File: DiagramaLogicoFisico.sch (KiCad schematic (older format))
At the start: 18 parts, among them J1 Conn_01x02, J2 Conn_01x03, J3 Conn_01x03, J4 Conn_01x04, J5 Conn_01x05, U1 TC1262-33, U2 DSPIC33EP128GM604, Y1 7Mhz

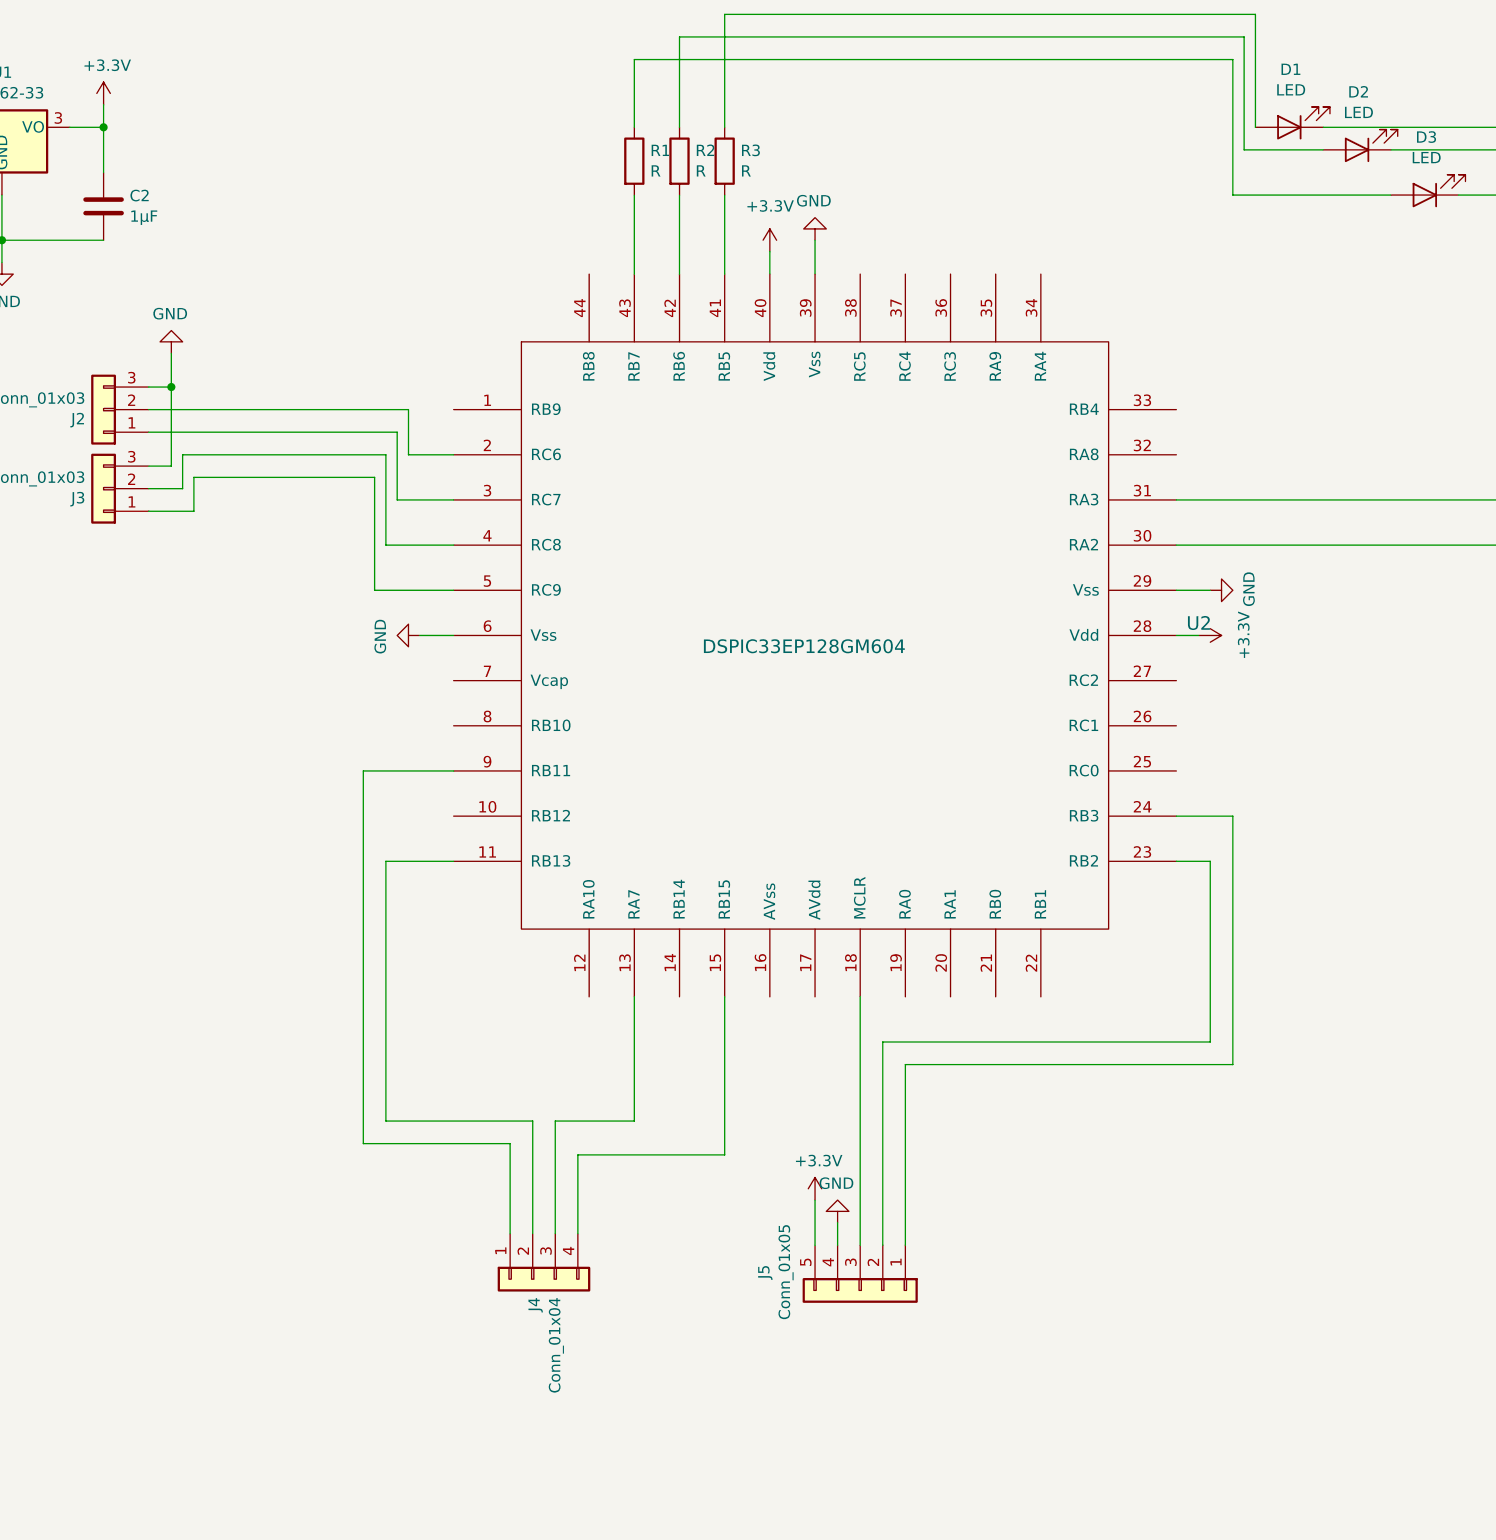
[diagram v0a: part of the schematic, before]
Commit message: Añadidos condensadores a pines de alimentación
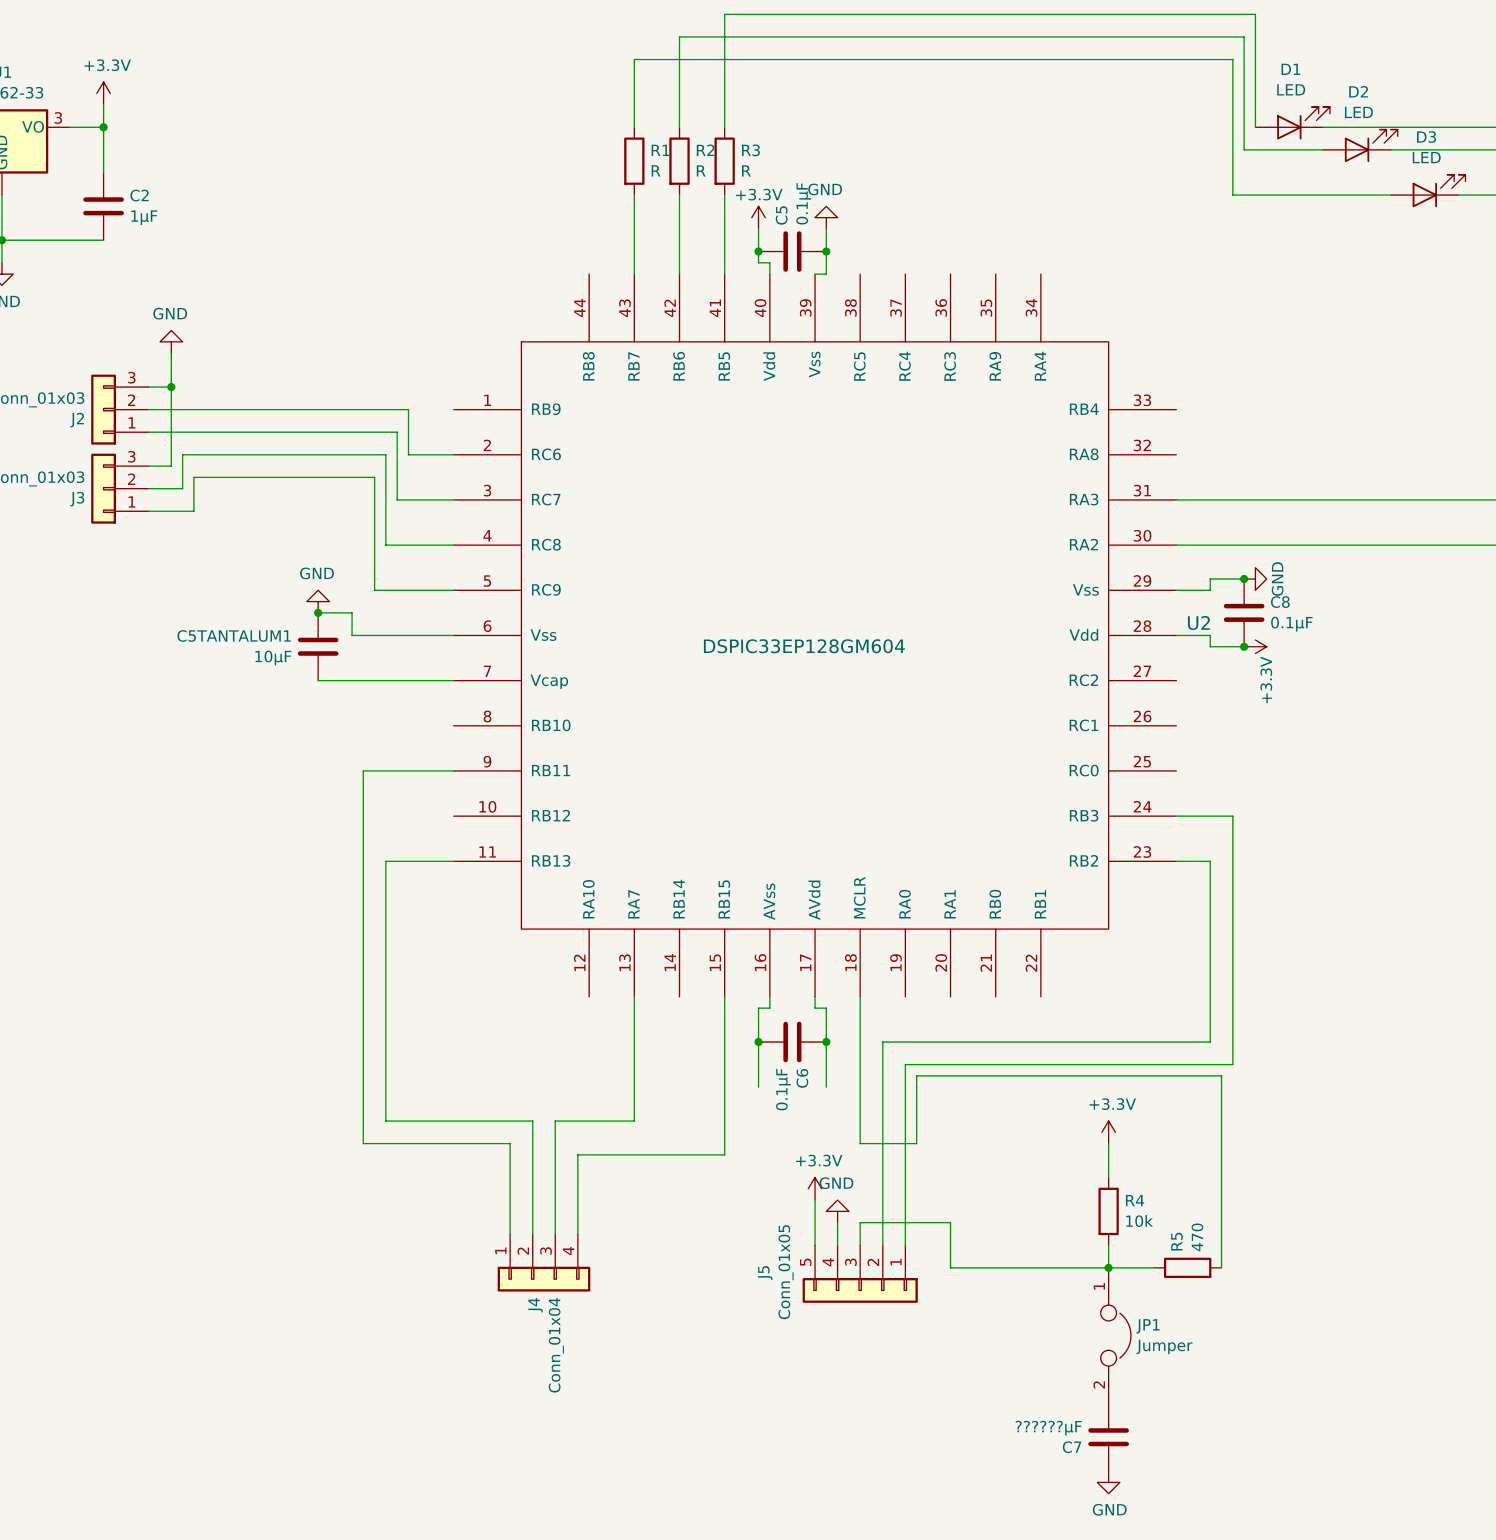
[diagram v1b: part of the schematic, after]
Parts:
- added C5, C6, C8: 0.1µF, Capacitor_THT:C_Disc_D3.8mm_W2.6mm_P2.50mm, symbol Device:C
- added C5TANTALUM1: 10µF, symbol Device:C
- added C7: ??????µF, symbol Device:C
- added JP1: Jumper, symbol Device:Jumper
- added R4: 10k, Resistor_THT:R_Axial_DIN0204_L3.6mm_D1.6mm_P5.08mm_Horizontal, symbol Device:R
- added R5: 470, Resistor_THT:R_Axial_DIN0204_L3.6mm_D1.6mm_P5.08mm_Horizontal, symbol Device:R
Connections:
- net +3V3: now also C5.1, C8.2, R4.1
- net GND: now also C5.2, C5TANTALUM1.1, C7.1, C8.1
- net at J5.3 (Pin_3): now also JP1.1, R4.2, R5.1; no longer U2.18 (MCLR)
- net at U2.16 (AVss): now also C6.2
- net at U2.17 (AVdd): now also C6.1
- net at U2.7 (Vcap): now also C5TANTALUM1.2
- new net: R5.2, U2.18 (MCLR)
- new net: C7.2, JP1.2

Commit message: Añadidos condensadores a pines de alimentación y establecido el circuito MCLR
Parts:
- removed C7: ??????µF, symbol Device:C
- removed JP1: Jumper, symbol Device:Jumper
- removed R5: 470, Resistor_THT:R_Axial_DIN0204_L3.6mm_D1.6mm_P5.08mm_Horizontal, symbol Device:R
- C5TANTALUM1: footprint (none) -> Capacitor_THT:C_Disc_D3.8mm_W2.6mm_P2.50mm
- R4: value 10k -> 5k
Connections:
- net +3V3: now also C6.1, U2.17 (AVdd)
- net GND: now also C6.2, U2.16 (AVss)
- net at J5.3 (Pin_3), R4.2: now also U2.18 (MCLR)
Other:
- moved on the sheet: C1, C2, J1, U1
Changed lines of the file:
@@
 $EndDescr
-$Comp
-L power:GND #PWR0101
-U 1 1 5E50C240
-P 12900 10000
-F 0 "#PWR0101" H 12900 9750 50  0001 C CNN
-F 1 "GND" H 12905 9827 50  0000 C CNN
-F 2 "" H 12900 10000 50  0001 C CNN
-F 3 "" H 12900 10000 50  0001 C CNN
-	1    12900 10000
-	1    0    0    -1
-$EndComp
 $Comp
 L Connector_Generic:Conn_01x03 J2
@@
 Wire Wire Line
 	15700 9700 15700 10050
-Connection ~ 13350 9400
-Wire Wire Line
-	13350 9400 13350 9300
-$Comp
-L power:+3.3V #PWR0102
-U 1 1 5E51D43F
-P 13350 9300
-F 0 "#PWR0102" H 13350 9150 50  0001 C CNN
-F 1 "+3.3V" H 13365 9473 50  0000 C CNN
-F 2 "" H 13350 9300 50  0001 C CNN
-F 3 "" H 13350 9300 50  0001 C CNN
-	1    13350 9300
-	1    0    0    -1
-$EndComp
-Connection ~ 12400 9900
-Wire Wire Line
-	11950 9900 12400 9900
-Wire Wire Line
-	11950 9500 11950 9900
-Connection ~ 12400 9400
-Wire Wire Line
-	11950 9400 12400 9400
-$Comp
-L Connector_Generic:Conn_01x02 J1
-U 1 1 5E51059C
-P 11750 9500
-F 0 "J1" H 11830 9492 50  0000 L CNN
-F 1 "Conn_01x02" H 11830 9401 50  0000 L CNN
-F 2 "TerminalBlock:TerminalBlock_bornier-2_P5.08mm" H 11750 9500 50  0001 C CNN
-F 3 "~" H 11750 9500 50  0001 C CNN
-	1    11750 9500
-	-1   0    0    1
-$EndComp
-Wire Wire Line
-	12900 9900 12900 10000
-$Comp
-L Device:C C1
-U 1 1 5E4F8296
-P 12400 9750
-F 0 "C1" H 12515 9796 50  0000 L CNN
-F 1 "1µF" H 12515 9705 50  0000 L CNN
-F 2 "" H 12438 9600 50  0001 C CNN
-F 3 "~" H 12400 9750 50  0001 C CNN
-	1    12400 9750
-	1    0    0    -1
-$EndComp
-Wire Wire Line
-	13350 9600 13350 9400
-Wire Wire Line
-	12400 9600 12400 9400
-Wire Wire Line
-	12400 9900 12900 9900
-Connection ~ 12900 9900
-Wire Wire Line
-	13200 9400 13350 9400
-Wire Wire Line
-	12900 9700 12900 9900
-Wire Wire Line
-	13350 9900 12900 9900
-Wire Wire Line
-	12400 9400 12600 9400
-$Comp
-L Device:C C2
-U 1 1 5E4EDB08
-P 13350 9750
-F 0 "C2" H 13465 9796 50  0000 L CNN
-F 1 "1µF" H 13465 9705 50  0000 L CNN
-F 2 "" H 13388 9600 50  0001 C CNN
-F 3 "~" H 13350 9750 50  0001 C CNN
-	1    13350 9750
-	1    0    0    -1
-$EndComp
-$Comp
-L Regulator_Linear:TC1262-33 U1
-U 1 1 5E50B885
-P 12900 9400
-F 0 "U1" H 12900 9642 50  0000 C CNN
-F 1 "TC1262-33" H 12900 9551 50  0000 C CNN
-F 2 "" H 12900 9625 50  0001 C CIN
-F 3 "http://ww1.microchip.com/downloads/en/DeviceDoc/21373C.pdf" H 12900 9100 50  0001 C CNN
-	1    12900 9400
-	1    0    0    -1
-$EndComp
 Wire Wire Line
 	14500 12250 14900 12250
@@
 F 0 "C5TANTALUM1" H 14415 11746 50  0000 L CNN
 F 1 "10µF" H 14415 11655 50  0000 L CNN
-F 2 "" H 14338 11550 50  0001 C CNN
+F 2 "Capacitor_THT:C_Disc_D3.8mm_W2.6mm_P2.50mm" H 14338 11550 50  0001 C CNN
 F 3 "~" H 14300 11700 50  0001 C CNN
 	1    14300 11700
@@
 Wire Wire Line
 	16900 13550 16900 14350
+Wire Wire Line
+	16700 14350 16700 14250
+Wire Wire Line
+	16700 14250 17100 14250
+Wire Wire Line
+	17100 14250 17100 14450
+Wire Wire Line
+	18300 13600 16950 13600
+Wire Wire Line
+	16950 13600 16950 13900
+Wire Wire Line
+	16950 13900 16700 13900
+Wire Wire Line
+	16700 13900 16700 13250
+$Comp
+L Device:R R2
+U 1 1 5E723556
+P 15900 9550
+F 0 "R2" H 15970 9596 50  0000 L CNN
+F 1 "R" H 15970 9505 50  0000 L CNN
+F 2 "Resistor_THT:R_Axial_DIN0204_L3.6mm_D1.6mm_P5.08mm_Horizontal" V 15830 9550 50  0001 C CNN
+F 3 "~" H 15900 9550 50  0001 C CNN
+	1    15900 9550
+	1    0    0    -1
+$EndComp
+Wire Wire Line
+	18300 14450 18300 13600
+Wire Wire Line
+	17100 14450 17800 14450
+Connection ~ 17800 14450
+Wire Wire Line
+	17800 14350 17800 14450
+Wire Wire Line
+	17800 13900 17800 14050
+$Comp
+L Device:R R4
+U 1 1 5E81C5AF
+P 17800 14200
+F 0 "R4" H 17870 14246 50  0000 L CNN
+F 1 "5k" H 17870 14155 50  0000 L CNN
+F 2 "Resistor_THT:R_Axial_DIN0204_L3.6mm_D1.6mm_P5.08mm_Horizontal" V 17730 14200 50  0001 C CNN
+F 3 "~" H 17800 14200 50  0001 C CNN
+	1    17800 14200
+	1    0    0    -1
+$EndComp
 $Comp
 L power:+3.3V #PWR0113
@@
 	1    0    0    -1
 $EndComp
-$Comp
-L Device:R R4
-U 1 1 5E81C5AF
-P 17800 14200
-F 0 "R4" H 17870 14246 50  0000 L CNN
-F 1 "10k" H 17870 14155 50  0000 L CNN
-F 2 "Resistor_THT:R_Axial_DIN0204_L3.6mm_D1.6mm_P5.08mm_Horizontal" V 17730 14200 50  0001 C CNN
-F 3 "~" H 17800 14200 50  0001 C CNN
-	1    17800 14200
-	1    0    0    -1
-$EndComp
-$Comp
-L Device:R R5
-U 1 1 5E81DAC6
-P 18150 14450
-F 0 "R5" H 18220 14496 50  0000 L CNN
-F 1 "470" H 18220 14405 50  0000 L CNN
-F 2 "Resistor_THT:R_Axial_DIN0204_L3.6mm_D1.6mm_P5.08mm_Horizontal" V 18080 14450 50  0001 C CNN
-F 3 "~" H 18150 14450 50  0001 C CNN
-	1    18150 14450
-	0    -1   -1   0
-$EndComp
-Wire Wire Line
-	17800 13900 17800 14050
-Wire Wire Line
-	17800 14450 18000 14450
-Wire Wire Line
-	17800 14350 17800 14450
-$Comp
-L Device:Jumper JP1
-U 1 1 5E838A4D
-P 17800 14750
-F 0 "JP1" V 17754 14877 50  0000 L CNN
-F 1 "Jumper" V 17845 14877 50  0000 L CNN
-F 2 "" H 17800 14750 50  0001 C CNN
-F 3 "~" H 17800 14750 50  0001 C CNN
-	1    17800 14750
-	0    1    1    0
-$EndComp
-Connection ~ 17800 14450
-$Comp
-L Device:C C7
-U 1 1 5E839BF2
-P 17800 15200
-F 0 "C7" H 17915 15246 50  0000 L CNN
-F 1 "??????µF" H 17915 15155 50  0000 L CNN
-F 2 "" H 17838 15050 50  0001 C CNN
-F 3 "~" H 17800 15200 50  0001 C CNN
-	1    17800 15200
-	-1   0    0    1
-$EndComp
+Wire Wire Line
+	17800 14450 18300 14450
 $Comp
 L power:GND #PWR0114
-U 1 1 5E83B128
-P 17800 15350
-F 0 "#PWR0114" H 17800 15100 50  0001 C CNN
-F 1 "GND" H 17805 15177 50  0000 C CNN
-F 2 "" H 17800 15350 50  0001 C CNN
-F 3 "" H 17800 15350 50  0001 C CNN
-	1    17800 15350
-	1    0    0    -1
-$EndComp
-Wire Wire Line
-	16700 14350 16700 14250
-Wire Wire Line
-	16700 14250 17100 14250
-Wire Wire Line
-	17100 14250 17100 14450
-Wire Wire Line
-	17100 14450 17800 14450
-Wire Wire Line
-	18300 14450 18300 13600
-Wire Wire Line
-	18300 13600 16950 13600
-Wire Wire Line
-	16950 13600 16950 13900
-Wire Wire Line
-	16950 13900 16700 13900
-Wire Wire Line
-	16700 13900 16700 13250
-$Comp
-L Device:R R2
-U 1 1 5E723556
-P 15900 9550
-F 0 "R2" H 15970 9596 50  0000 L CNN
-F 1 "R" H 15970 9505 50  0000 L CNN
-F 2 "Resistor_THT:R_Axial_DIN0204_L3.6mm_D1.6mm_P5.08mm_Horizontal" V 15830 9550 50  0001 C CNN
-F 3 "~" H 15900 9550 50  0001 C CNN
-	1    15900 9550
-	1    0    0    -1
+U 1 1 5E7D0D32
+P 16250 13650
+F 0 "#PWR0114" H 16250 13400 50  0001 C CNN
+F 1 "GND" H 16255 13477 50  0000 C CNN
+F 2 "" H 16250 13650 50  0001 C CNN
+F 3 "" H 16250 13650 50  0001 C CNN
+	1    16250 13650
+	1    0    0    -1
+$EndComp
+$Comp
+L power:+3.3V #PWR0115
+U 1 1 5E7D1F3B
+P 16550 13650
+F 0 "#PWR0115" H 16550 13500 50  0001 C CNN
+F 1 "+3.3V" H 16700 13750 50  0000 C CNN
+F 2 "" H 16550 13650 50  0001 C CNN
+F 3 "" H 16550 13650 50  0001 C CNN
+	1    16550 13650
+	-1   0    0    1
+$EndComp
+$Comp
+L power:GND #PWR0101
+U 1 1 5E50C240
+P 2400 1600
+F 0 "#PWR0101" H 2400 1350 50  0001 C CNN
+F 1 "GND" H 2405 1427 50  0000 C CNN
+F 2 "" H 2400 1600 50  0001 C CNN
+F 3 "" H 2400 1600 50  0001 C CNN
+	1    2400 1600
+	1    0    0    -1
+$EndComp
+$Comp
+L power:+3.3V #PWR0102
+U 1 1 5E51D43F
+P 2850 900
+F 0 "#PWR0102" H 2850 750 50  0001 C CNN
+F 1 "+3.3V" H 2865 1073 50  0000 C CNN
+F 2 "" H 2850 900 50  0001 C CNN
+F 3 "" H 2850 900 50  0001 C CNN
+	1    2850 900
+	1    0    0    -1
+$EndComp
+Wire Wire Line
+	2400 1500 2400 1600
+Wire Wire Line
+	1450 1500 1900 1500
+Wire Wire Line
+	1900 1500 2400 1500
+Connection ~ 1900 1500
+$Comp
+L Device:C C1
+U 1 1 5E4F8296
+P 1900 1350
+F 0 "C1" H 2015 1396 50  0000 L CNN
+F 1 "1µF" H 2015 1305 50  0000 L CNN
+F 2 "" H 1938 1200 50  0001 C CNN
+F 3 "~" H 1900 1350 50  0001 C CNN
+	1    1900 1350
+	1    0    0    -1
+$EndComp
+Wire Wire Line
+	1450 1000 1900 1000
+Wire Wire Line
+	1900 1000 2100 1000
+Connection ~ 1900 1000
+Wire Wire Line
+	1900 1200 1900 1000
+Connection ~ 2400 1500
+Wire Wire Line
+	2850 1500 2400 1500
+Wire Wire Line
+	2850 1000 2850 900
+Wire Wire Line
+	2850 1200 2850 1000
+Connection ~ 2850 1000
+Wire Wire Line
+	2700 1000 2850 1000
+Wire Wire Line
+	2400 1300 2400 1500
+$Comp
+L Device:C C2
+U 1 1 5E4EDB08
+P 2850 1350
+F 0 "C2" H 2965 1396 50  0000 L CNN
+F 1 "1µF" H 2965 1305 50  0000 L CNN
+F 2 "" H 2888 1200 50  0001 C CNN
+F 3 "~" H 2850 1350 50  0001 C CNN
+	1    2850 1350
+	1    0    0    -1
+$EndComp
+$Comp
+L Regulator_Linear:TC1262-33 U1
+U 1 1 5E50B885
+P 2400 1000
+F 0 "U1" H 2400 1242 50  0000 C CNN
+F 1 "TC1262-33" H 2400 1151 50  0000 C CNN
+F 2 "" H 2400 1225 50  0001 C CIN
+F 3 "http://ww1.microchip.com/downloads/en/DeviceDoc/21373C.pdf" H 2400 700 50  0001 C CNN
+	1    2400 1000
+	1    0    0    -1
+$EndComp
+Wire Wire Line
+	1450 1100 1450 1500
+$Comp
+L Connector_Generic:Conn_01x02 J1
+U 1 1 5E51059C
+P 1250 1100
+F 0 "J1" H 1330 1092 50  0000 L CNN
+F 1 "Conn_01x02" H 1330 1001 50  0000 L CNN
+F 2 "TerminalBlock:TerminalBlock_bornier-2_P5.08mm" H 1250 1100 50  0001 C CNN
+F 3 "~" H 1250 1100 50  0001 C CNN
+	1    1250 1100
+	-1   0    0    1
 $EndComp
 $EndSCHEMATC
